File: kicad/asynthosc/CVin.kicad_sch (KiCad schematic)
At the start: 11 parts, among them J14 AudioJack3, SW4 SW_DIP_x02, U9 MCP6004

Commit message: sch: pcb: fix: footprint mismatches
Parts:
- D24: footprint SOT-23-6 -> Package_TO_SOT_SMD:SOT-23-6
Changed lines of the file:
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@@
 			)
 		)
-		(property "Footprint" "SOT-23-6"
+		(property "Footprint" "Package_TO_SOT_SMD:SOT-23-6"
 			(at 138.43 54.61 0)
 			(effects

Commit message: bom: update mfr, serials and lcsc fields
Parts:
- D24: LCSC (none) -> C154909; Manufacturer (none) -> Diodes, Inc; RefNum (none) -> SD103ASDM-7-F
- J14: LCSC (none) -> C381132
- SW4: LCSC (none) -> C6709488; Manufacturer (none) -> SHOU HAN; RefNum (none) -> 2.54-2P TPPT
- U9: LCSC (none) -> C627416
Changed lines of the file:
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@@
+			)
+		)
+		(property "LCSC" "C154909"
+			(at 138.43 54.61 0)
+			(effects
+				(font
+					(size 1.27 1.27)
+				)
+				(hide yes)
+			)
+		)
+		(property "Manufacturer" "Diodes, Inc"
+			(at 138.43 54.61 0)
+			(effects
+				(font
+					(size 1.27 1.27)
+				)
+				(hide yes)
+			)
+		)
+		(property "RefNum" "SD103ASDM-7-F"
+			(at 138.43 54.61 0)
+			(effects
+				(font
+					(size 1.27 1.27)
+				)
+				(hide yes)
 			)
 		)
@@
 			)
 		)
+		(property "LCSC" "C6709488"
+			(at 62.23 38.1 0)
+			(effects
+				(font
+					(size 1.27 1.27)
+				)
+				(hide yes)
+			)
+		)
+		(property "Manufacturer" "SHOU HAN"
+			(at 62.23 38.1 0)
+			(effects
+				(font
+					(size 1.27 1.27)
+				)
+				(hide yes)
+			)
+		)
+		(property "RefNum" "2.54-2P TPPT"
+			(at 62.23 38.1 0)
+			(effects
+				(font
+					(size 1.27 1.27)
+				)
+				(hide yes)
+			)
+		)
 		(pin "4"
 		)
@@
 			)
 		)
-		(property "LCSC" ""
+		(property "LCSC" "C381132"
 			(at 39.37 54.61 0)
 			(effects
@@
 			)
 		)
-		(property "LCSC" ""
-			(at 113.03 54.61 0)
-			(effects
+		(property "LCSC" "C627416"
+			(at 113.03 54.61 0)
+			(effects

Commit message: bom: sch: pcb: update for sourcing in jlc pcba services
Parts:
- SW4: LCSC C6709488 -> C18198124; Manufacturer SHOU HAN -> Hanbo; RefNum 2.54-2P TPPT -> DO-02PD
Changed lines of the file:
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@@
 			)
 		)
-		(property "LCSC" "C6709488"
+		(property "LCSC" "C18198124"
 			(at 62.23 38.1 0)
 			(effects
@@
 			)
 		)
-		(property "Manufacturer" "SHOU HAN"
+		(property "Manufacturer" "Hanbo"
 			(at 62.23 38.1 0)
 			(effects
@@
 			)
 		)
-		(property "RefNum" "2.54-2P TPPT"
+		(property "RefNum" "DO-02PD"
 			(at 62.23 38.1 0)
 			(effects

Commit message: bom: add jlcpcb field with simplified footprint
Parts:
- C50: JLC (none) -> 0603
- D24: JLC (none) -> SOT-23-6
- R70, R71, R72, R73, R74, R75: JLC (none) -> 0402
- U9: JLC (none) -> TSSOP-14
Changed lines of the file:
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@@
+			)
+		)
+		(property "JLC" "0402"
+			(at 113.03 41.91 0)
+			(effects
+				(font
+					(size 1.27 1.27)
+				)
+				(hide yes)
 			)
 		)
@@
 		)
 		(property "RefNum" "_generic_"
+			(at 55.88 52.07 0)
+			(effects
+				(font
+					(size 1.27 1.27)
+				)
+				(hide yes)
+			)
+		)
+		(property "JLC" "0402"
 			(at 55.88 52.07 0)
 			(effects
@@
 			)
 		)
+		(property "JLC" "SOT-23-6"
+			(at 138.43 54.61 0)
+			(effects
+				(font
+					(size 1.27 1.27)
+				)
+				(hide yes)
+			)
+		)
 		(pin "3"
 		)
@@
 			)
 		)
+		(property "JLC" ""
+			(at 62.23 38.1 0)
+			(effects
+				(font
+					(size 1.27 1.27)
+				)
+				(hide yes)
+			)
+		)
 		(pin "4"
 		)
@@
 			)
 		)
+		(property "JLC" ""
+			(at 39.37 54.61 0)
+			(effects
+				(font
+					(size 1.27 1.27)
+				)
+				(hide yes)
+			)
+		)
 		(pin "S"
 		)
@@
 			)
 		)
+		(property "JLC" "TSSOP-14"
+			(at 113.03 54.61 0)
+			(effects
+				(font
+					(size 1.27 1.27)
+				)
+				(hide yes)
+			)
+		)
 		(pin "1"
 		)
@@
 			)
 		)
+		(property "JLC" "0603"
+			(at 113.03 33.02 0)
+			(effects
+				(font
+					(size 1.27 1.27)
+				)
+				(hide yes)
+			)
+		)
 		(pin "1"
 		)
@@
 			)
 		)
+		(property "JLC" "0402"
+			(at 92.71 57.15 0)
+			(effects
+				(font
+					(size 1.27 1.27)
+				)
+				(hide yes)
+			)
+		)
 		(pin "1"
 		)
@@
 			)
 		)
+		(property "JLC" "0402"
+			(at 68.58 59.69 0)
+			(effects
+				(font
+					(size 1.27 1.27)
+				)
+				(hide yes)
+			)
+		)
 		(pin "1"
 		)
@@
 		)
 		(property "RefNum" "_generic_"
+			(at 101.6 64.77 0)
+			(effects
+				(font
+					(size 1.27 1.27)
+				)
+				(hide yes)
+			)
+		)
+		(property "JLC" "0402"
 			(at 101.6 64.77 0)
 			(effects
@@
 			(at 87.63 52.07 0)
 			(effects
+				(font
+					(size 1.27 1.27)
+				)
+				(hide yes)
+			)
+		)
+		(property "JLC" "0402"
+			(at 87.63 52.07 0)
+			(effects

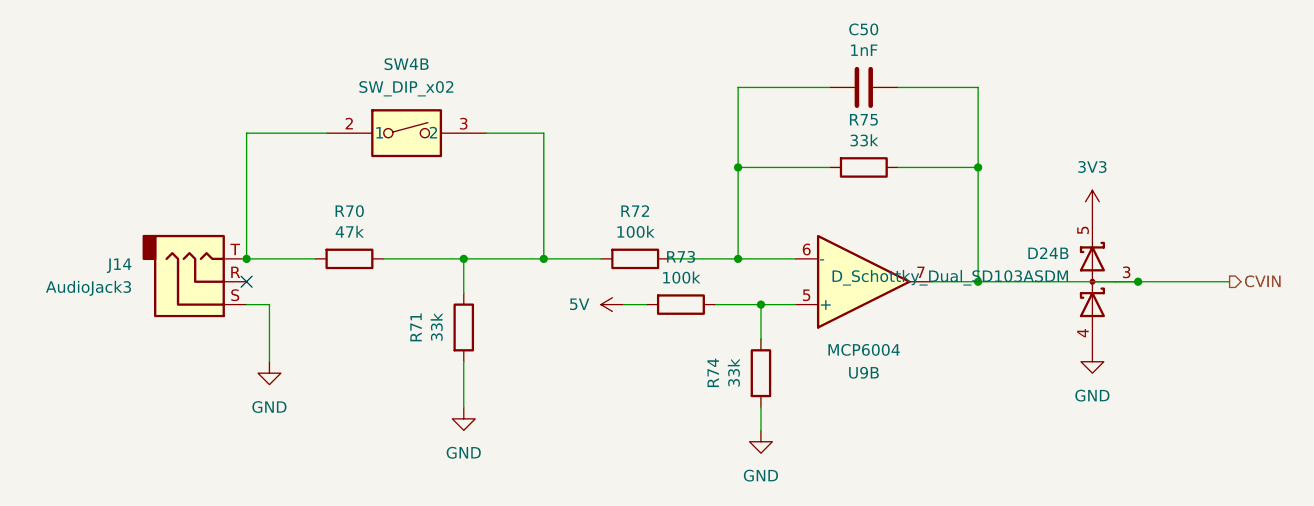
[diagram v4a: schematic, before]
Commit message: bom: dnp for all manually equiped components
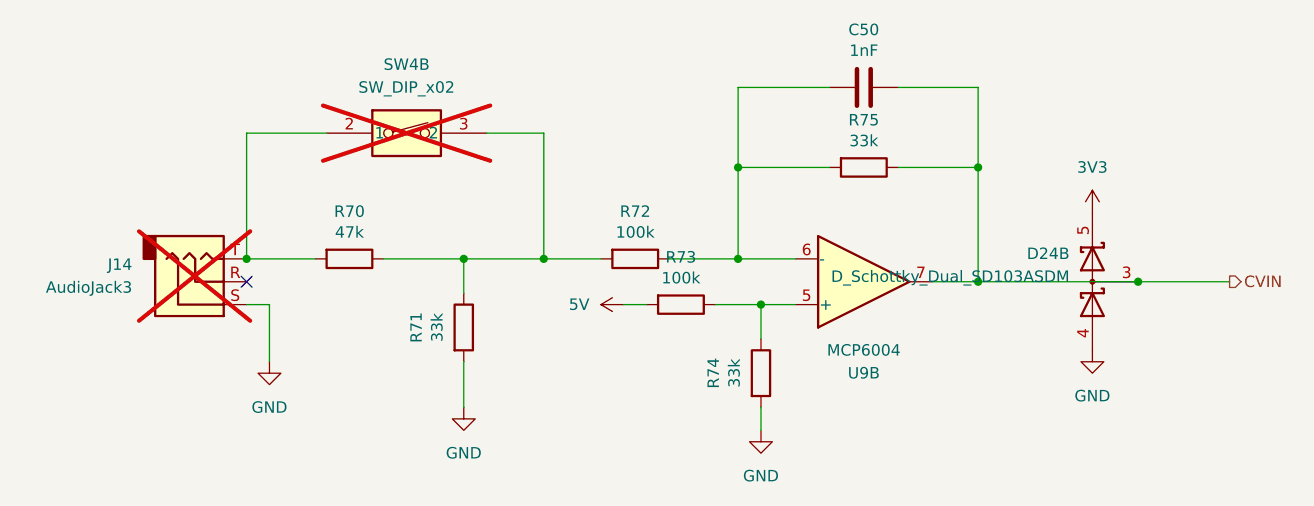
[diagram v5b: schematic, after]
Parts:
- J14, SW4: now not fitted
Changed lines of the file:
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@@
 		(in_bom yes)
 		(on_board yes)
-		(dnp no)
+		(dnp yes)
 		(fields_autoplaced yes)
 		(property "Reference" "SW4"
@@
 		(in_bom yes)
 		(on_board yes)
-		(dnp no)
+		(dnp yes)
 		(property "Reference" "J14"
 			(at 31.75 52.7049 0)

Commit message: bom: adding jlc ref to generic
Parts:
- C50: LCSC (none) -> C1588
- R70: LCSC (none) -> C25792
- R71, R74, R75: LCSC (none) -> C25779
- R72, R73: LCSC (none) -> C25741
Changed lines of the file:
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@@
 			)
 		)
-		(property "LCSC" ""
+		(property "LCSC" "C25779"
 			(at 113.03 41.91 0)
 			(effects
@@
 			)
 		)
-		(property "LCSC" ""
+		(property "LCSC" "C25792"
 			(at 55.88 52.07 0)
 			(effects
@@
 			)
 		)
-		(property "LCSC" ""
+		(property "LCSC" "C1588"
 			(at 113.03 33.02 0)
 			(effects
@@
 			)
 		)
-		(property "LCSC" ""
+		(property "LCSC" "C25741"
 			(at 92.71 57.15 0)
 			(effects
@@
 			)
 		)
-		(property "LCSC" ""
+		(property "LCSC" "C25779"
 			(at 68.58 59.69 0)
 			(effects
@@
 			)
 		)
-		(property "LCSC" ""
+		(property "LCSC" "C25779"
 			(at 101.6 64.77 0)
 			(effects
@@
 			)
 		)
-		(property "LCSC" ""
+		(property "LCSC" "C25741"
 			(at 87.63 52.07 0)
 			(effects

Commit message: sch: update bom
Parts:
- SW4: now fitted
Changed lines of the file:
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@@
 		(in_bom yes)
 		(on_board yes)
-		(dnp yes)
+		(dnp no)
 		(fields_autoplaced yes)
 		(property "Reference" "SW4"
